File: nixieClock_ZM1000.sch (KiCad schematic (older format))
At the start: 0 parts

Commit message: no message
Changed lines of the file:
@@
 $Descr A4 11693 8268
 encoding utf-8
-Sheet 1 3
+Sheet 1 5
 Title ""
 Date ""
@@
 $EndDescr
 $Sheet
-S 1750 750  700  350
-U 5D8D3E88
+S 3000 5500 5000 500
+U 5D904EA9
+F0 "Tubes" 50
+F1 "Tubes.sch" 50
+$EndSheet
+$Sheet
+S 3000 4500 5000 500
+U 5D90512A
+F0 "Shift Registers" 50
+F1 "Shift.sch" 50
+$EndSheet
+$Sheet
+S 3000 3000 1000 1000
+U 5D90562D
+F0 "PSU" 50
+F1 "PSU.sch" 50
+F2 "HV" O L 3000 3800 50
+F3 "3V3" O R 4000 3800 50
+F4 "5V" O L 3000 3650 50
+F5 "Vin" I L 3000 3150 50
+$EndSheet
+$Sheet
+S 6000 3000 2000 1000
+U 5D9058C6
 F0 "Control" 50
 F1 "Control.sch" 50
 $EndSheet
-$Sheet
-S 750  750  800  350
-U 5D8D5A25
-F0 "PSU" 50
-F1 "PSUsch.sch" 50
-$EndSheet
+Wire Wire Line
+	3000 3150 2250 3150
+Text Label 2250 3150 0    50   ~ 0
+??????
 $EndSCHEMATC

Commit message: no message
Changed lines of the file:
@@
 $EndDescr
 $Sheet
-S 3000 5500 5000 500
+S 1450 750  1000 1000
+U 5D90562D
+F0 "PSU" 50
+F1 "PSU.sch" 50
+F2 "HV" O L 1450 1550 50
+F3 "3V3" O R 2450 1550 50
+F4 "5V" O L 1450 1650 50
+F5 "Vin" I L 1450 900 50
+$EndSheet
+$Sheet
+S 4950 2400 1050 1450
+U 5D9058C6
+F0 "Control (ADU)" 50
+F1 "Control.sch" 50
+F2 "BLANK" I L 4950 2800 50
+F3 "TUBETX" I L 4950 2700 50
+F4 "SHIFTCLK" I L 4950 2950 50
+F5 "STORAGECLK" I L 4950 3050 50
+F6 "5V" I L 4950 2550 50
+F7 "DP6" I L 4950 3750 50
+F8 "DP5" I L 4950 3650 50
+F9 "DP4" I L 4950 3550 50
+F10 "DP3" I L 4950 3450 50
+F11 "DP2" I L 4950 3350 50
+F12 "DP1" I L 4950 3250 50
+$EndSheet
+Wire Wire Line
+	1450 900  700  900
+Text Label 700  900  0    50   ~ 0
+??????
+$Sheet
+S 1450 2400 1050 3450
 U 5D904EA9
 F0 "Tubes" 50
 F1 "Tubes.sch" 50
+F2 "5V" I L 1450 2550 50
+F3 "HV" I L 1450 2650 50
+F4 "BCD_T1A" I R 2500 2550 50
+F5 "BCD_T1B" I R 2500 2650 50
+F6 "BCD_T1C" I R 2500 2750 50
+F7 "BCD_T5A" I R 2500 4350 50
+F8 "BCD_T5B" I R 2500 4450 50
+F9 "BCD_T5C" I R 2500 4550 50
+F10 "BCD_T5D" I R 2500 4650 50
+F11 "BCD_T4A" I R 2500 3900 50
+F12 "BCD_T4B" I R 2500 4000 50
+F13 "BCD_T4C" I R 2500 4100 50
+F14 "BCD_T4D" I R 2500 4200 50
+F15 "BCD_T1D" I R 2500 2850 50
+F16 "BCD_T2A" I R 2500 3000 50
+F17 "BCD_T2B" I R 2500 3100 50
+F18 "BCD_T2C" I R 2500 3200 50
+F19 "BCD_T2D" I R 2500 3300 50
+F20 "BCD_T3A" I R 2500 3450 50
+F21 "BCD_T3B" I R 2500 3550 50
+F22 "BCD_T3C" I R 2500 3650 50
+F23 "BCD_T3D" I R 2500 3750 50
+F24 "DP1" I R 2500 5250 50
+F25 "DP2" I R 2500 5350 50
+F26 "DP3" I R 2500 5450 50
+F27 "DP6" I R 2500 5750 50
+F28 "DP5" I R 2500 5650 50
+F29 "DP4" I R 2500 5550 50
+F30 "BCD_T6A" I R 2500 4800 50
+F31 "BCD_T6B" I R 2500 4900 50
+F32 "BCD_T6C" I R 2500 5000 50
+F33 "BCD_T6D" I R 2500 5100 50
 $EndSheet
 $Sheet
-S 3000 4500 5000 500
-U 5D90512A
+S 3250 2400 1000 2800
+U 5DB44C0F
 F0 "Shift Registers" 50
-F1 "Shift.sch" 50
-$EndSheet
-$Sheet
-S 3000 3000 1000 1000
-U 5D90562D
-F0 "PSU" 50
-F1 "PSU.sch" 50
-F2 "HV" O L 3000 3800 50
-F3 "3V3" O R 4000 3800 50
-F4 "5V" O L 3000 3650 50
-F5 "Vin" I L 3000 3150 50
-$EndSheet
-$Sheet
-S 6000 3000 2000 1000
-U 5D9058C6
-F0 "Control" 50
-F1 "Control.sch" 50
+F1 "Shift_Registers.sch" 50
+F2 "5V" I R 4250 2550 50
+F3 "BCD_T1A" I L 3250 2550 50
+F4 "BCD_T1B" I L 3250 2650 50
+F5 "BCD_T1C" I L 3250 2750 50
+F6 "BCD_T5A" I L 3250 4350 50
+F7 "BCD_T5B" I L 3250 4450 50
+F8 "BCD_T5C" I L 3250 4550 50
+F9 "BCD_T5D" I L 3250 4650 50
+F10 "BCD_T4A" I L 3250 3900 50
+F11 "BCD_T4B" I L 3250 4000 50
+F12 "BCD_T4C" I L 3250 4100 50
+F13 "BCD_T4D" I L 3250 4200 50
+F14 "BCD_T1D" I L 3250 2850 50
+F15 "BCD_T2A" I L 3250 3000 50
+F16 "BCD_T2B" I L 3250 3100 50
+F17 "BCD_T2C" I L 3250 3200 50
+F18 "BCD_T2D" I L 3250 3300 50
+F19 "BCD_T3A" I L 3250 3450 50
+F20 "BCD_T3B" I L 3250 3550 50
+F21 "BCD_T3C" I L 3250 3650 50
+F22 "BCD_T3D" I L 3250 3750 50
+F23 "BCD_T6A" I L 3250 4800 50
+F24 "BCD_T6B" I L 3250 4900 50
+F25 "BCD_T6C" I L 3250 5000 50
+F26 "BCD_T6D" I L 3250 5100 50
+F27 "BLANK" I R 4250 2800 50
+F28 "TUBETX" I R 4250 2700 50
+F29 "SHIFTCLK" I R 4250 2950 50
+F30 "STORAGECLK" I R 4250 3050 50
 $EndSheet
 Wire Wire Line
-	3000 3150 2250 3150
-Text Label 2250 3150 0    50   ~ 0
-??????
+	2500 2550 3250 2550
+Wire Wire Line
+	2500 2650 3250 2650
+Wire Wire Line
+	2500 2750 3250 2750
+Wire Wire Line
+	2500 2850 3250 2850
+Wire Wire Line
+	2500 3000 3250 3000
+Wire Wire Line
+	2500 3100 3250 3100
+Wire Wire Line
+	2500 3200 3250 3200
+Wire Wire Line
+	2500 3300 3250 3300
+Wire Wire Line
+	2500 3450 3250 3450
+Wire Wire Line
+	2500 3550 3250 3550
+Wire Wire Line
+	2500 3650 3250 3650
+Wire Wire Line
+	2500 3750 3250 3750
+Wire Wire Line
+	2500 3900 3250 3900
+Wire Wire Line
+	2500 4000 3250 4000
+Wire Wire Line
+	2500 4100 3250 4100
+Wire Wire Line
+	2500 4200 3250 4200
+Wire Wire Line
+	2500 4350 3250 4350
+Wire Wire Line
+	2500 4450 3250 4450
+Wire Wire Line
+	2500 4550 3250 4550
+Wire Wire Line
+	2500 4650 3250 4650
+Wire Wire Line
+	2500 4800 3250 4800
+Wire Wire Line
+	2500 4900 3250 4900
+Wire Wire Line
+	2500 5000 3250 5000
+Wire Wire Line
+	2500 5100 3250 5100
+Wire Wire Line
+	1150 1550 1150 2650
+Wire Wire Line
+	1150 2650 1450 2650
+Wire Wire Line
+	1150 1550 1450 1550
+Wire Wire Line
+	1450 2550 1250 2550
+Wire Wire Line
+	1250 1650 1450 1650
+Wire Wire Line
+	4250 2950 4950 2950
+Wire Wire Line
+	4950 3050 4250 3050
+Wire Wire Line
+	4250 2800 4950 2800
+Wire Wire Line
+	4950 2700 4250 2700
+Wire Wire Line
+	1250 1650 1250 2050
+Wire Wire Line
+	4250 2550 4600 2550
+Wire Wire Line
+	4600 2550 4600 2050
+Wire Wire Line
+	4600 2050 1250 2050
+Connection ~ 4600 2550
+Wire Wire Line
+	4600 2550 4950 2550
+Connection ~ 1250 2050
+Wire Wire Line
+	1250 2050 1250 2550
 $EndSCHEMATC

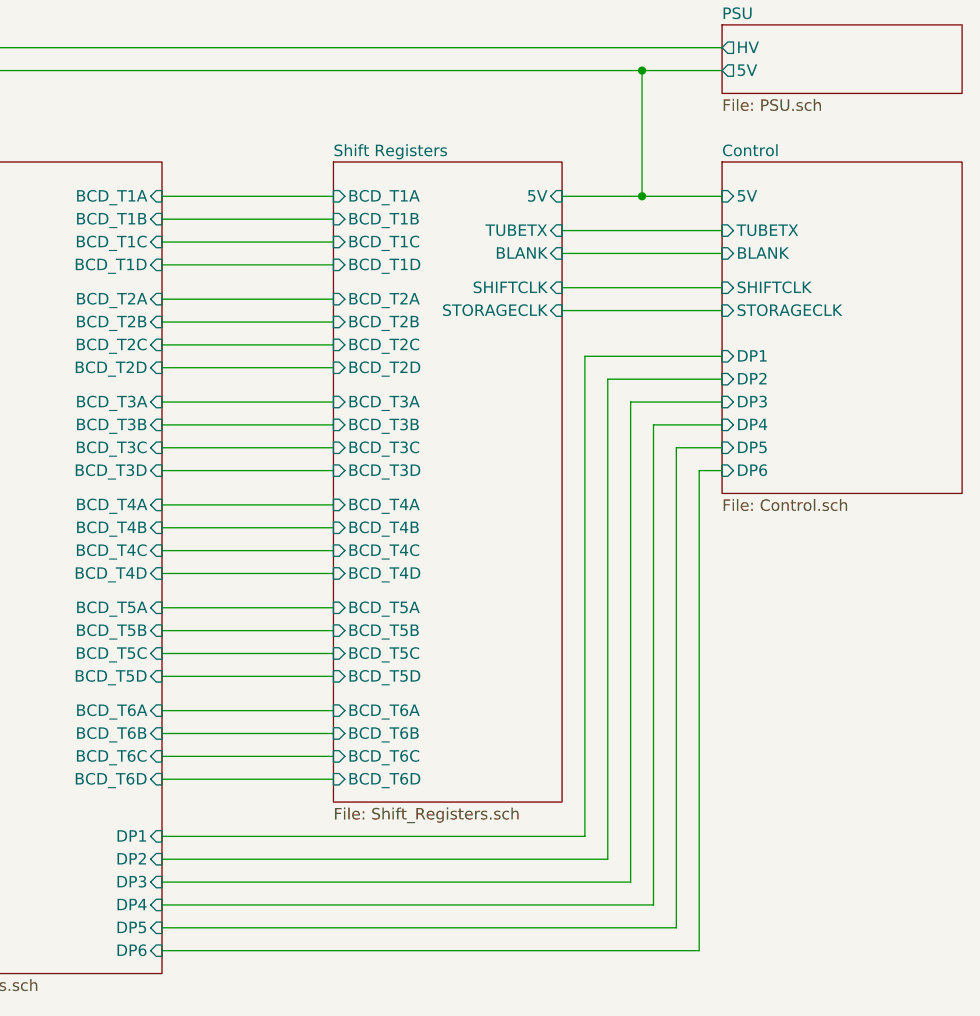
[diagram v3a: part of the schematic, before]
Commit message: Moved DPs to shift register as not enough IO
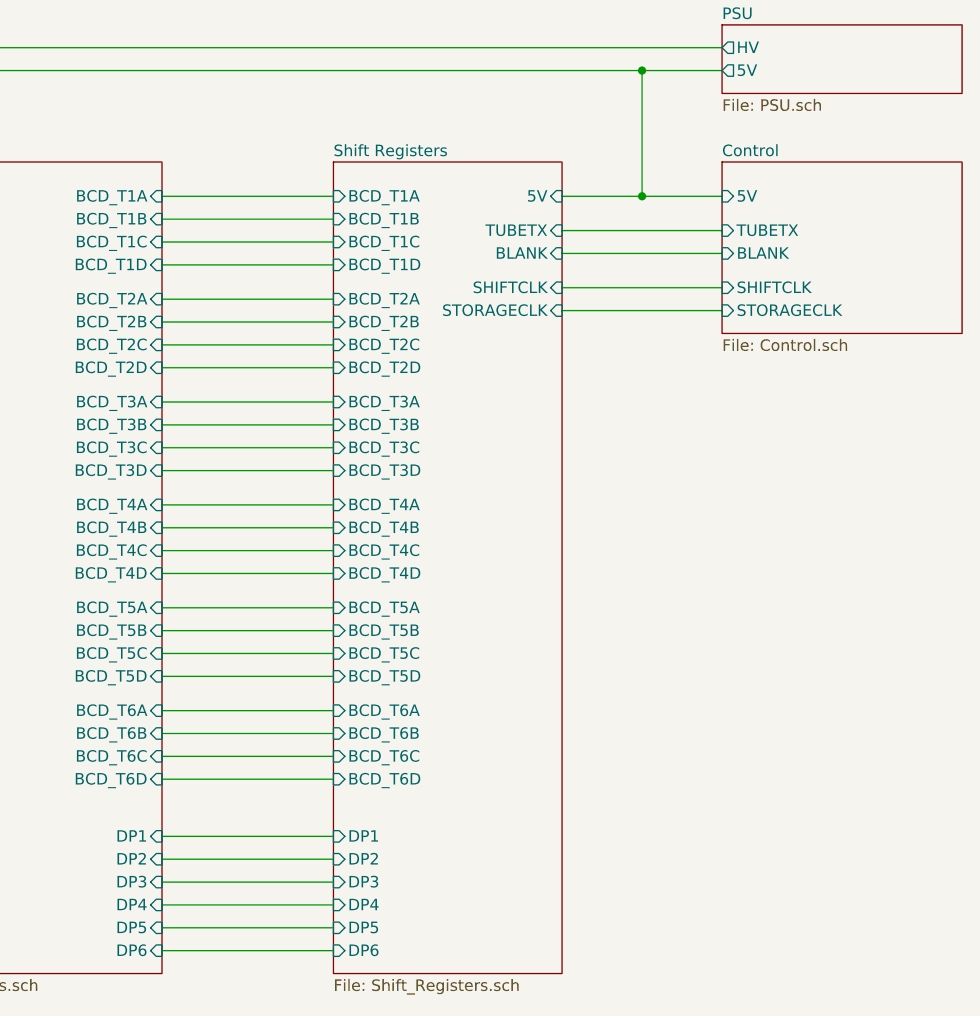
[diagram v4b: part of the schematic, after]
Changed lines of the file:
@@
 $EndDescr
 $Sheet
-S 7100 2550 1050 1450
+S 7100 2550 1050 750
 U 5D9058C6
 F0 "Control" 50
@@
 F5 "STORAGECLK" I L 7100 3200 50
 F6 "5V" I L 7100 2700 50
-F7 "DP6" I L 7100 3900 50
-F8 "DP5" I L 7100 3800 50
-F9 "DP4" I L 7100 3700 50
-F10 "DP3" I L 7100 3600 50
-F11 "DP2" I L 7100 3500 50
-F12 "DP1" I L 7100 3400 50
 $EndSheet
 $Sheet
@@
 $EndSheet
 $Sheet
-S 5400 2550 1000 2800
+S 5400 2550 1000 3550
 U 5DB44C0F
 F0 "Shift Registers" 50
@@
 F29 "SHIFTCLK" I R 6400 3100 50
 F30 "STORAGECLK" I R 6400 3200 50
+F31 "DP6" I L 5400 6000 50
+F32 "DP5" I L 5400 5900 50
+F33 "DP4" I L 5400 5800 50
+F34 "DP3" I L 5400 5700 50
+F35 "DP2" I L 5400 5600 50
+F36 "DP1" I L 5400 5500 50
 $EndSheet
 Wire Wire Line
@@
 Wire Wire Line
 	7100 2850 6400 2850
-Wire Wire Line
-	7100 3400 6500 3400
-Wire Wire Line
-	7100 3500 6600 3500
-Wire Wire Line
-	6700 3600 7100 3600
-Wire Wire Line
-	7100 3700 6800 3700
-Wire Wire Line
-	6900 3800 7100 3800
-Wire Wire Line
-	7100 3900 7000 3900
-Wire Wire Line
-	6500 5500 4650 5500
-Wire Wire Line
-	6500 3400 6500 5500
-Wire Wire Line
-	4650 5600 6600 5600
-Wire Wire Line
-	6600 3500 6600 5600
-Wire Wire Line
-	4650 5700 6700 5700
-Wire Wire Line
-	6700 3600 6700 5700
-Wire Wire Line
-	4650 5800 6800 5800
-Wire Wire Line
-	6800 3700 6800 5800
-Wire Wire Line
-	4650 5900 6900 5900
-Wire Wire Line
-	6900 3800 6900 5900
-Wire Wire Line
-	4650 6000 7000 6000
-Wire Wire Line
-	7000 3900 7000 6000
 $Sheet
 S 7100 1950 1050 300
@@
 Wire Wire Line
 	3300 2050 3300 2800
+Wire Wire Line
+	4650 5500 5400 5500
+Wire Wire Line
+	5400 5600 4650 5600
+Wire Wire Line
+	4650 5700 5400 5700
+Wire Wire Line
+	5400 5800 4650 5800
+Wire Wire Line
+	4650 5900 5400 5900
+Wire Wire Line
+	5400 6000 4650 6000
 $EndSCHEMATC

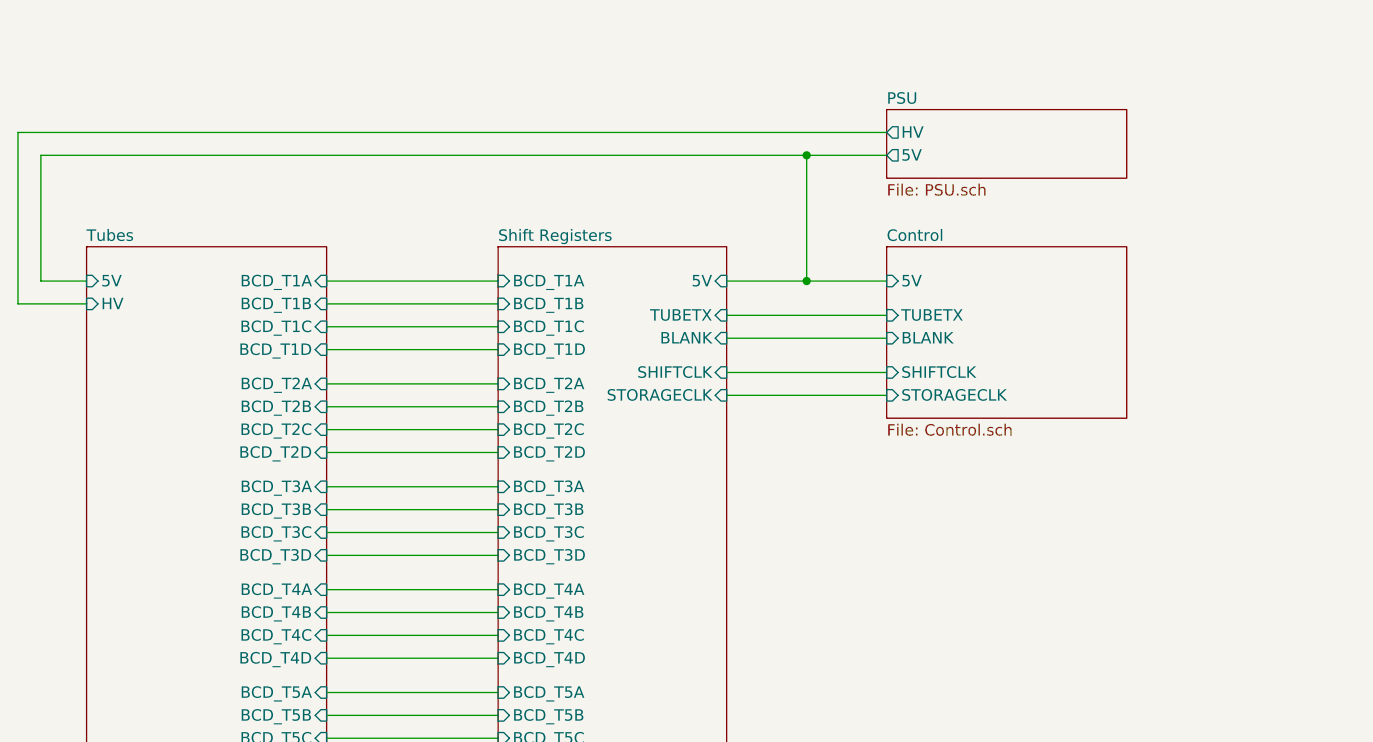
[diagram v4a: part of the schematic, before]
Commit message: Completed layout inc optimisation of data pattern for shift registers
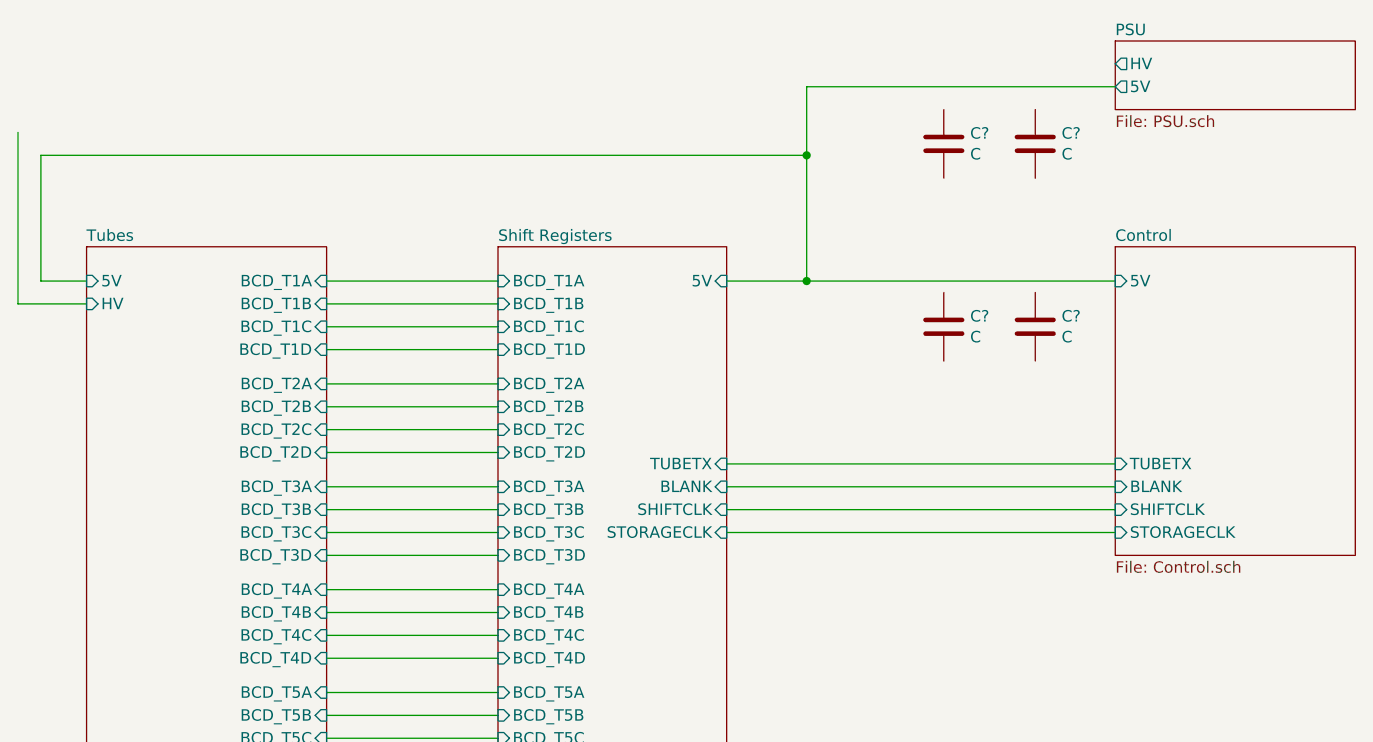
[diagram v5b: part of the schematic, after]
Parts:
- added C? (x4): C, symbol Device:C
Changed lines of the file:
@@
 $EndDescr
 $Sheet
-S 7100 2550 1050 750
+S 8100 2550 1050 1350
 U 5D9058C6
 F0 "Control" 50
 F1 "Control.sch" 50
-F2 "BLANK" I L 7100 2950 50
-F3 "TUBETX" I L 7100 2850 50
-F4 "SHIFTCLK" I L 7100 3100 50
-F5 "STORAGECLK" I L 7100 3200 50
-F6 "5V" I L 7100 2700 50
+F2 "BLANK" I L 8100 3600 50
+F3 "TUBETX" I L 8100 3500 50
+F4 "SHIFTCLK" I L 8100 3700 50
+F5 "STORAGECLK" I L 8100 3800 50
+F6 "5V" I L 8100 2700 50
 $EndSheet
 $Sheet
@@
 F25 "BCD_T6C" I L 5400 5150 50
 F26 "BCD_T6D" I L 5400 5250 50
-F27 "BLANK" I R 6400 2950 50
-F28 "TUBETX" I R 6400 2850 50
-F29 "SHIFTCLK" I R 6400 3100 50
-F30 "STORAGECLK" I R 6400 3200 50
+F27 "BLANK" I R 6400 3600 50
+F28 "TUBETX" I R 6400 3500 50
+F29 "SHIFTCLK" I R 6400 3700 50
+F30 "STORAGECLK" I R 6400 3800 50
 F31 "DP6" I L 5400 6000 50
 F32 "DP5" I L 5400 5900 50
@@
 Wire Wire Line
 	3600 2700 3400 2700
-Wire Wire Line
-	6400 3100 7100 3100
-Wire Wire Line
-	7100 3200 6400 3200
-Wire Wire Line
-	6400 2950 7100 2950
-Wire Wire Line
-	7100 2850 6400 2850
-$Sheet
-S 7100 1950 1050 300
+$Sheet
+S 8100 1650 1050 300
 U 5D90562D
 F0 "PSU" 50
 F1 "PSU.sch" 50
-F2 "HV" O L 7100 2050 50
-F3 "5V" O L 7100 2150 50
+F2 "HV" O L 8100 1750 50
+F3 "5V" O L 8100 1850 50
 $EndSheet
 Wire Wire Line
 	6400 2700 6750 2700
-Wire Wire Line
-	7100 2150 6750 2150
 Wire Wire Line
 	6750 2150 6750 2700
 Connection ~ 6750 2700
 Wire Wire Line
-	6750 2700 7100 2700
-Wire Wire Line
-	6750 2150 3400 2150
+	3400 2150 3400 2700
+Wire Wire Line
+	3300 2050 3300 2800
+Wire Wire Line
+	4650 5500 5400 5500
+Wire Wire Line
+	5400 5600 4650 5600
+Wire Wire Line
+	4650 5700 5400 5700
+Wire Wire Line
+	5400 5800 4650 5800
+Wire Wire Line
+	4650 5900 5400 5900
+Wire Wire Line
+	5400 6000 4650 6000
+Wire Wire Line
+	6400 3800 8100 3800
+Wire Wire Line
+	8100 3700 6400 3700
+Wire Wire Line
+	6400 3600 8100 3600
+Wire Wire Line
+	8100 3500 6400 3500
+Wire Wire Line
+	6750 2700 8100 2700
+Wire Wire Line
+	3400 2150 6750 2150
+Wire Wire Line
+	6750 2150 6750 1850
+Wire Wire Line
+	6750 1850 8100 1850
 Connection ~ 6750 2150
-Wire Wire Line
-	3400 2150 3400 2700
-Wire Wire Line
-	7100 2050 3300 2050
-Wire Wire Line
-	3300 2050 3300 2800
-Wire Wire Line
-	4650 5500 5400 5500
-Wire Wire Line
-	5400 5600 4650 5600
-Wire Wire Line
-	4650 5700 5400 5700
-Wire Wire Line
-	5400 5800 4650 5800
-Wire Wire Line
-	4650 5900 5400 5900
-Wire Wire Line
-	5400 6000 4650 6000
+$Comp
+L Device:C C?
+U 1 1 5DA9F019
+P 7750 2900
+F 0 "C?" H 7865 2946 50  0000 L CNN
+F 1 "C" H 7865 2855 50  0000 L CNN
+F 2 "" H 7788 2750 50  0001 C CNN
+F 3 "~" H 7750 2900 50  0001 C CNN
+	1    7750 2900
+	1    0    0    -1
+$EndComp
+$Comp
+L Device:C C?
+U 1 1 5DA9F705
+P 7350 2900
+F 0 "C?" H 7465 2946 50  0000 L CNN
+F 1 "C" H 7465 2855 50  0000 L CNN
+F 2 "" H 7388 2750 50  0001 C CNN
+F 3 "~" H 7350 2900 50  0001 C CNN
+	1    7350 2900
+	1    0    0    -1
+$EndComp
+$Comp
+L Device:C C?
+U 1 1 5DAA0435
+P 7750 2100
+F 0 "C?" H 7865 2146 50  0000 L CNN
+F 1 "C" H 7865 2055 50  0000 L CNN
+F 2 "" H 7788 1950 50  0001 C CNN
+F 3 "~" H 7750 2100 50  0001 C CNN
+	1    7750 2100
+	1    0    0    -1
+$EndComp
+$Comp
+L Device:C C?
+U 1 1 5DAA043B
+P 7350 2100
+F 0 "C?" H 7465 2146 50  0000 L CNN
+F 1 "C" H 7465 2055 50  0000 L CNN
+F 2 "" H 7388 1950 50  0001 C CNN
+F 3 "~" H 7350 2100 50  0001 C CNN
+	1    7350 2100
+	1    0    0    -1
+$EndComp
 $EndSCHEMATC
